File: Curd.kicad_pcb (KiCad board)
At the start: 4 copper layers, 65 parts, among them Q1 RQ3E120AT, Q10 PMV40UN2, Q11 RQ3E120AT, Q12 PMV40UN2, Q13 RQ3E120AT, Q14 PMV40UN2, Q15 RQ3E120AT, Q16 PMV40UN2, Q2 PMV40UN2, Q3 RQ3E120AT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

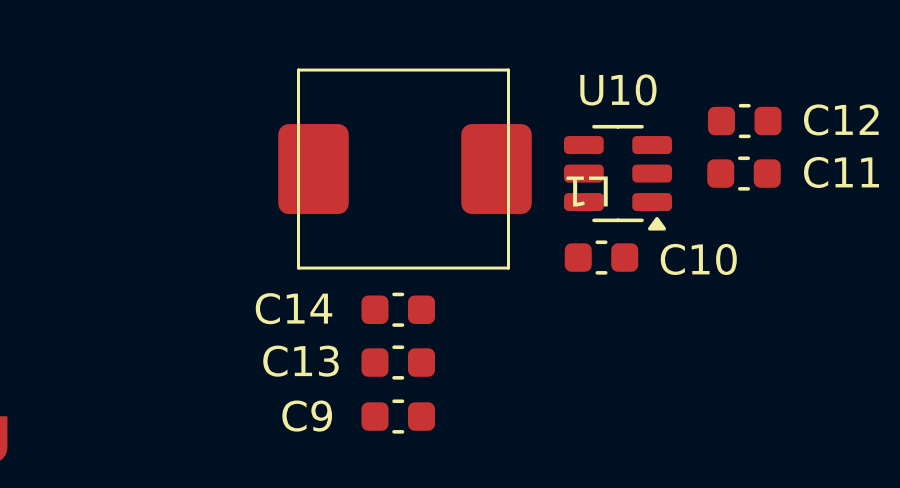
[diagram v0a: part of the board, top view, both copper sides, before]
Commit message: KiCad git plugin
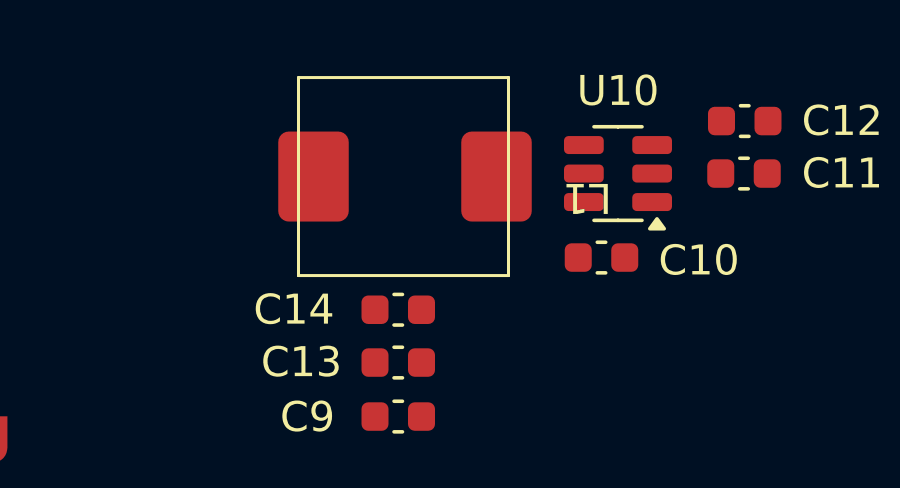
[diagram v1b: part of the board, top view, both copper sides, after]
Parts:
- moved L1 0.25 mm to (131.8, 33.8)
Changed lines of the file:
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@@
 	(footprint "Curd:XR0630-4R7M"
 		(layer "F.Cu")
-		(at 131.75 33.5 180)
+		(at 131.75 33.75 180)
 		(property "Reference" "L1"
 			(at -6.025 -0.51 180)

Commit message: Added routing
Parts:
- removed C12: 22uF, Capacitor_SMD:C_0603_1608Metric
- added R25: ~, Resistor_SMD:R_0603_1608Metric, F.Cu at (79.0, 52.2)
- added R26: ~, Resistor_SMD:R_0603_1608Metric, F.Cu at (98.0, 52.0)
- added R27: ~, Resistor_SMD:R_0603_1608Metric, F.Cu at (115.8, 51.9)
- added R28: ~, Resistor_SMD:R_0603_1608Metric, F.Cu at (133.5, 52.0)
- added R29: ~, Resistor_SMD:R_0603_1608Metric, F.Cu at (79.0, 67.5)
- added R30: ~, Resistor_SMD:R_0603_1608Metric, F.Cu at (98.2, 67.3)
- added R31: ~, Resistor_SMD:R_0603_1608Metric, F.Cu at (115.8, 67.7)
- added R32: ~, Resistor_SMD:R_0603_1608Metric, F.Cu at (133.5, 67.2)
- C11: value 22uF -> 10uF
- moved C13 22.8 mm to (109.3, 34.5), turned to 90 degrees
- moved C14 20.7 mm to (111.1, 34.5), turned to 90 degrees
- moved C11 17.1 mm to (127.2, 40.0), turned to 0 degrees
- moved C9 8.56 mm to (137.2, 35.2), turned to 90 degrees
- moved C10 5.13 mm to (133.4, 38.0)
- moved U10 5.06 mm to (134.1, 35.2)
- moved L1 4.83 mm to (127.2, 35.5)
- moved U3 1.38 mm to (110.3, 39.1)
- moved R14 1.25 mm to (87.7, 64.5), turned to 90 degrees
- moved C5 1.23 mm to (82.3, 73.3)
- moved U6 1.23 mm to (84.5, 69.4)
- moved Q10 1.23 mm to (84.5, 64.5)
- moved Q9 1.23 mm to (98.8, 70.3)
- moved R13 1.23 mm to (91.5, 67.3), turned to 180 degrees
- moved R15 1.23 mm to (81.5, 64.5)
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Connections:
- C1 pad 1: AVDD -> V_IN
- C2 pad 1: AVDD -> V_IN
- C3 pad 1: AVDD -> V_IN
- C4 pad 1: AVDD -> V_IN
- C5 pad 1: AVDD -> V_IN
- C6 pad 1: AVDD -> V_IN
- C7 pad 1: AVDD -> V_IN
- C8 pad 1: AVDD -> V_IN
- Q1 pad 1: Net-(U1A-+) -> Net-(U1A--)
- Q1 pad 2: Net-(U1A-+) -> Net-(U1A--)
- Q1 pad 3: Net-(U1A-+) -> Net-(U1A--)
- Q10 pad 2: Net-(U6B-+) -> Net-(U6B--)
- Q10 pad 3: Net-(U6A--) -> Net-(U6A-+)
- Q11 pad 1: Net-(U7A-+) -> Net-(U7A--)
- Q11 pad 2: Net-(U7A-+) -> Net-(U7A--)
- Q11 pad 3: Net-(U7A-+) -> Net-(U7A--)
- Q12 pad 2: Net-(U7B-+) -> Net-(U7B--)
- Q12 pad 3: Net-(U7A--) -> Net-(U7A-+)
- Q13 pad 1: Net-(U8A-+) -> Net-(U8A--)
- Q13 pad 2: Net-(U8A-+) -> Net-(U8A--)
- Q13 pad 3: Net-(U8A-+) -> Net-(U8A--)
- Q14 pad 3: Net-(U8A--) -> Net-(U8A-+)
- Q15 pad 1: Net-(U9A-+) -> Net-(U9A--)
- Q15 pad 2: Net-(U9A-+) -> Net-(U9A--)
- Q15 pad 3: Net-(U9A-+) -> Net-(U9A--)
- Q16 pad 2: Net-(U9B-+) -> Net-(U9B--)
- Q16 pad 3: Net-(U9A--) -> Net-(U9A-+)
- Q2 pad 2: Net-(U1B-+) -> Net-(U1B--)
- Q2 pad 3: Net-(U1A--) -> Net-(U1A-+)
- Q3 pad 1: Net-(U2A-+) -> Net-(U2A--)
- Q3 pad 2: Net-(U2A-+) -> Net-(U2A--)
- Q3 pad 3: Net-(U2A-+) -> Net-(U2A--)
- Q4 pad 2: Net-(U2B-+) -> Net-(U2B--)
- Q4 pad 3: Net-(U2A--) -> Net-(U2A-+)
- Q5 pad 1: Net-(U4A-+) -> Net-(U4A--)
- Q5 pad 2: Net-(U4A-+) -> Net-(U4A--)
- Q5 pad 3: Net-(U4A-+) -> Net-(U4A--)
- Q6 pad 2: Net-(U4B-+) -> Net-(U4B--)
- Q6 pad 3: Net-(U4A--) -> Net-(U4A-+)
- Q7 pad 1: Net-(U5A-+) -> Net-(U5A--)
- Q7 pad 2: Net-(U5A-+) -> Net-(U5A--)
- Q7 pad 3: Net-(U5A-+) -> Net-(U5A--)
- Q8 pad 2: Net-(U5B-+) -> Net-(U5B--)
- Q8 pad 3: Net-(U5A--) -> Net-(U5A-+)
- Q9 pad 1: Net-(U6A-+) -> Net-(U6A--)
- Q9 pad 2: Net-(U6A-+) -> Net-(U6A--)
- Q9 pad 3: Net-(U6A-+) -> Net-(U6A--)
- R1 pad 2: Net-(U1A--) -> Net-(U1A-+)
- R10 pad 2: Net-(U5A--) -> Net-(U5A-+)
- R11 pad 1: Net-(U5A-+) -> Net-(U5A--)
- R12 pad 1: Net-(U5B-+) -> Net-(U5B--)
- R13 pad 2: Net-(U6A--) -> Net-(U6A-+)
- R14 pad 1: Net-(U6A-+) -> Net-(U6A--)
- R15 pad 1: Net-(U6B-+) -> Net-(U6B--)
- R16 pad 2: Net-(U7A--) -> Net-(U7A-+)
- R17 pad 1: Net-(U7A-+) -> Net-(U7A--)
- R18 pad 1: Net-(U7B-+) -> Net-(U7B--)
- R19 pad 2: Net-(U8A--) -> Net-(U8A-+)
- R2 pad 1: Net-(U1A-+) -> Net-(U1A--)
- R20 pad 1: Net-(U8A-+) -> Net-(U8A--)
- R22 pad 2: Net-(U9A--) -> Net-(U9A-+)
- R23 pad 1: Net-(U9A-+) -> Net-(U9A--)
- R24 pad 1: Net-(U9B-+) -> Net-(U9B--)
- R3 pad 1: Net-(U1B-+) -> Net-(U1B--)
- R4 pad 2: Net-(U2A--) -> Net-(U2A-+)
- R5 pad 1: Net-(U2A-+) -> Net-(U2A--)
- R6 pad 1: Net-(U2B-+) -> Net-(U2B--)
- R7 pad 2: Net-(U4A--) -> Net-(U4A-+)
- R8 pad 1: Net-(U4A-+) -> Net-(U4A--)
- R9 pad 1: Net-(U4B-+) -> Net-(U4B--)
- U1 pad 5: Net-(U1B-+) -> DAC0
- U1 pad 6: DAC0 -> Net-(U1B--)
- U1 pad 8: AVDD -> V_IN
- U2 pad 5: Net-(U2B-+) -> DAC1
- U2 pad 6: DAC1 -> Net-(U2B--)
- U2 pad 8: AVDD -> V_IN
- U3 pad 10: DAC6 -> Net-(U3-OUT6)
- U3 pad 11: DAC7 -> Net-(U3-OUT7)
- U3 pad 2: DAC0 -> Net-(U3-OUT0)
- U3 pad 3: DAC1 -> Net-(U3-OUT1)
- U3 pad 4: DAC2 -> Net-(U3-OUT2)
- U3 pad 5: DAC3 -> Net-(U3-OUT3)
- U3 pad 8: DAC4 -> Net-(U3-OUT4)
- U3 pad 9: DAC5 -> Net-(U3-OUT5)
- U4 pad 5: Net-(U4B-+) -> DAC2
- U4 pad 6: DAC2 -> Net-(U4B--)
- U4 pad 8: AVDD -> V_IN
- U5 pad 5: Net-(U5B-+) -> DAC3
- U5 pad 6: DAC3 -> Net-(U5B--)
- U5 pad 8: AVDD -> V_IN
- U6 pad 5: Net-(U6B-+) -> DAC4
- U6 pad 6: DAC4 -> Net-(U6B--)
- U6 pad 8: AVDD -> V_IN
- U7 pad 5: Net-(U7B-+) -> DAC5
- U7 pad 6: DAC5 -> Net-(U7B--)
- U7 pad 8: AVDD -> V_IN
- U8 pad 8: AVDD -> V_IN
- U9 pad 5: Net-(U9B-+) -> DAC7
- U9 pad 6: DAC7 -> Net-(U9B--)
- U9 pad 8: AVDD -> V_IN
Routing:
- net V_IN: track 7.35 -> 537.2 mm
- net +3.3V: track 0.00 -> 14.8 mm
- net Net-(Q4-Pad1): track 0.00 -> 8.98 mm
- net Net-(U2A-+): track 0.00 -> 7.41 mm
- net Net-(U10-SW): track 0.00 -> 7.41 mm
- net Net-(U2B--): track 0.00 -> 6.88 mm
- net Net-(U5A-+): track 0.00 -> 5.89 mm
- net Net-(U1A-+): track 3.01 -> 8.83 mm
- net Net-(U1A--): track 10.2 -> 5.81 mm
- net Net-(U1B-+): track 4.24 -> 0.00 mm
- net Net-(U3-OUT7): track 0.00 -> 3.28 mm, vias 0 -> 1
- net Net-(U3-OUT6): track 0.00 -> 3.26 mm, vias 0 -> 1
- net Net-(U3-OUT2): track 0.00 -> 2.94 mm, vias 0 -> 1
- net Net-(U3-OUT1): track 0.00 -> 2.66 mm, vias 0 -> 1
- net Net-(U10-BST): track 0.00 -> 2.44 mm
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- added copper zone on F.Cu, net +3.3V
- added copper zone on F.Cu, net V_IN
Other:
- board outline added: 80 x 50 mm
- board text removed: "analog"

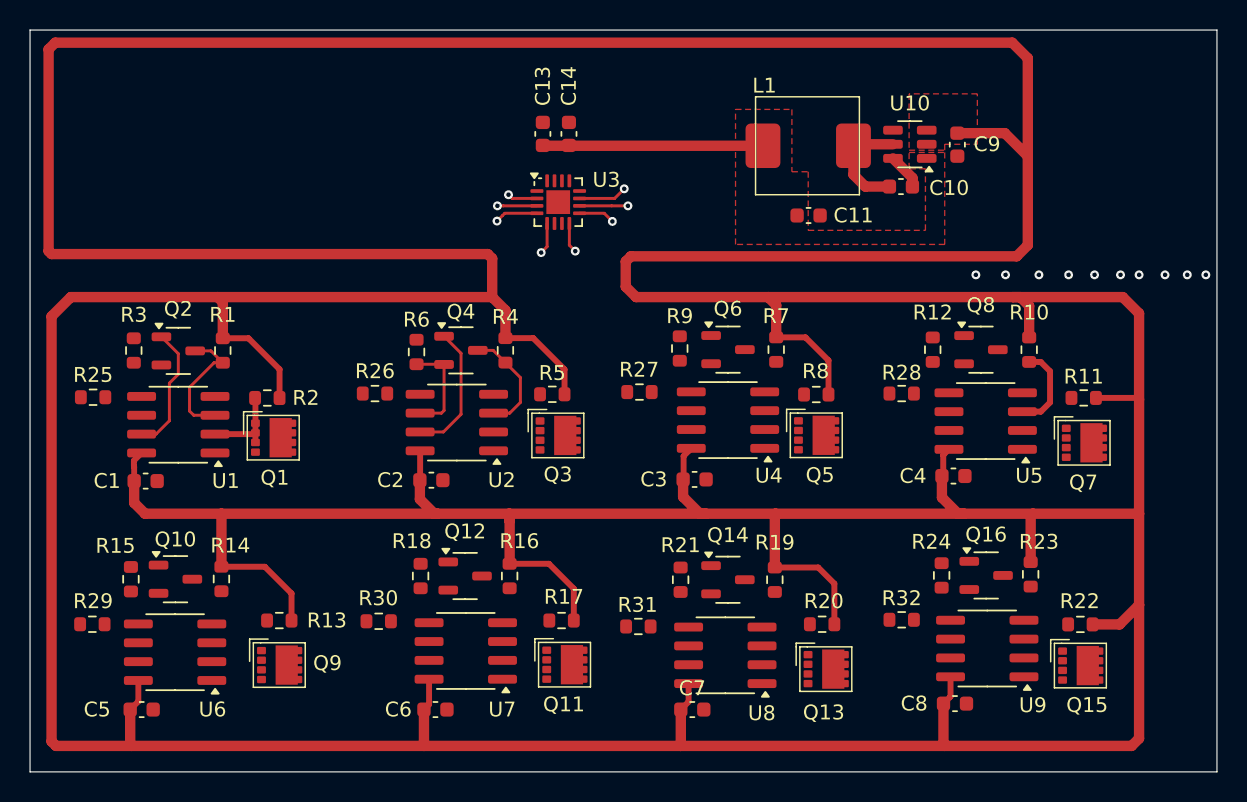
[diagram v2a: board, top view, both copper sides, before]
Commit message: Updated routing
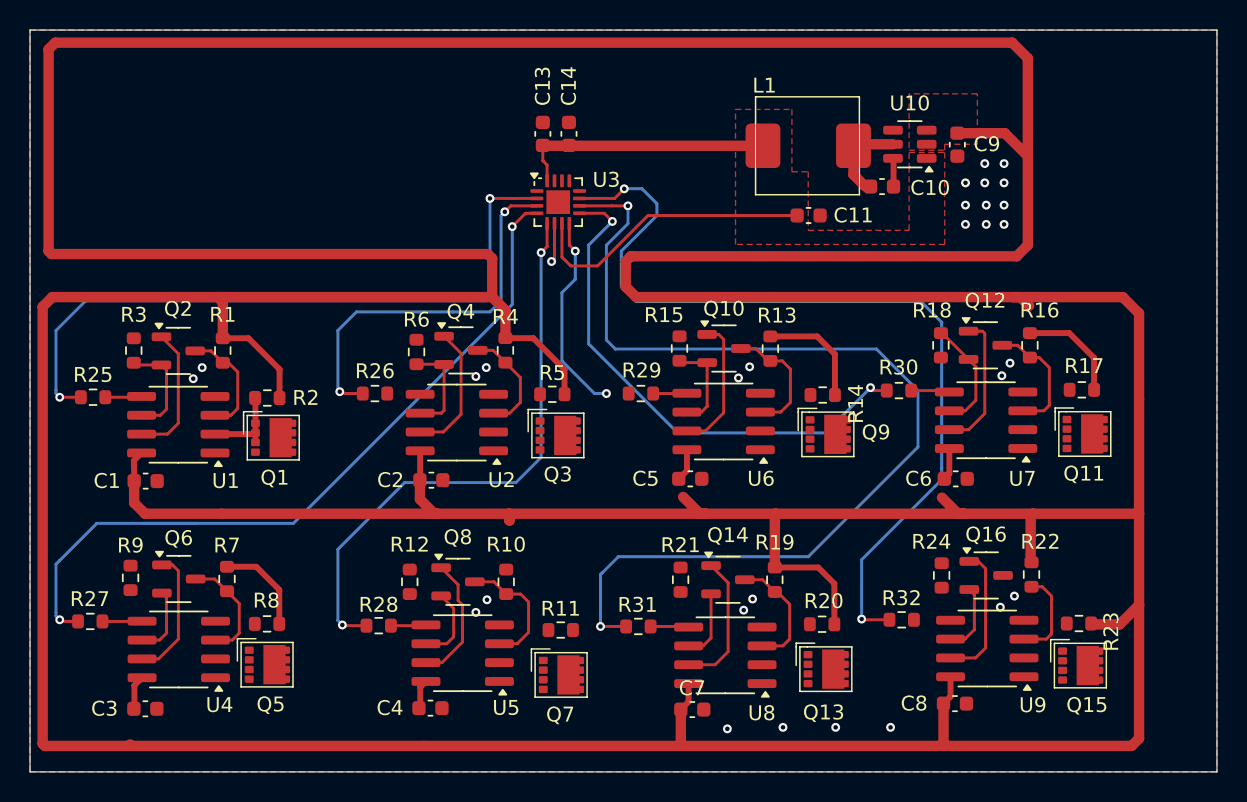
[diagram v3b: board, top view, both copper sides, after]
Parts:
- moved R14 42.4 mm to (128.2, 52.1), turned to 0 degrees
- moved Q5 40.1 mm to (98.0, 70.3)
- moved R8 40.1 mm to (90.7, 67.5)
- moved C3 40.1 mm to (82.5, 73.2)
- moved Q6 40.1 mm to (84.8, 64.5)
- moved R27 40.1 mm to (78.8, 67.4)
- moved R7 40.1 mm to (88.0, 64.5)
- moved R9 40.1 mm to (81.5, 64.4)
- moved U4 40.1 mm to (84.8, 69.2)
- moved Q10 40.1 mm to (121.5, 49.0)
- moved Q9 40.1 mm to (135.8, 54.8)
- moved R15 40.1 mm to (118.5, 49.0)
- moved C5 40.1 mm to (119.2, 57.8)
- moved R29 40.1 mm to (115.9, 52.0)
- moved U6 40.1 mm to (121.5, 53.9)
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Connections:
- C8 pad 2: unconnected-(C8-Pad2) -> GND
- R24 pad 2: unconnected-(R24-Pad2) -> GND
- U9 pad 4: unconnected-(U9C-V--Pad4) -> GND
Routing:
- net Net-(U3-OUT6): track 3.26 -> 69.3 mm, vias 1 -> 2
- net Net-(U3-OUT7): track 3.28 -> 59.2 mm, vias 1 -> 2
- net Net-(U3-OUT2): track 2.94 -> 53.9 mm, vias 1 -> 2
- net Net-(U3-OUT0): track 2.02 -> 46.1 mm, vias 1 -> 2
- net Net-(U3-OUT3): track 2.13 -> 39.1 mm, vias 1 -> 2
- net Net-(U3-OUT5): track 2.44 -> 35.3 mm, vias 1 -> 2
- net Net-(U3-OUT1): track 2.66 -> 26.0 mm, vias 1 -> 2
- net +3.3V: track 14.8 -> 37.1 mm
- net V_IN: track 537.2 -> 517.4 mm
- net Net-(U3-OUT4): track 2.03 -> 13.7 mm, vias 1 -> 2
- net Net-(Q12-Pad1): track 0.00 -> 9.39 mm
- net Net-(Q14-Pad1): track 0.00 -> 9.30 mm
- net Net-(Q16-Pad1): track 0.00 -> 9.28 mm
- net Net-(Q10-Pad1): track 0.00 -> 9.18 mm
- net Net-(Q6-Pad1): track 0.00 -> 8.88 mm
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- added copper zone on B.Cu, net GND
- added copper zone on F.Cu, net GND
- added copper zone on In1.Cu, net GND
